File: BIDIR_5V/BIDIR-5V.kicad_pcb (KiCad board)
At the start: 2 copper layers, 5 x 34 mm, 16 parts, among them U1 SN74LVC1T45DCK

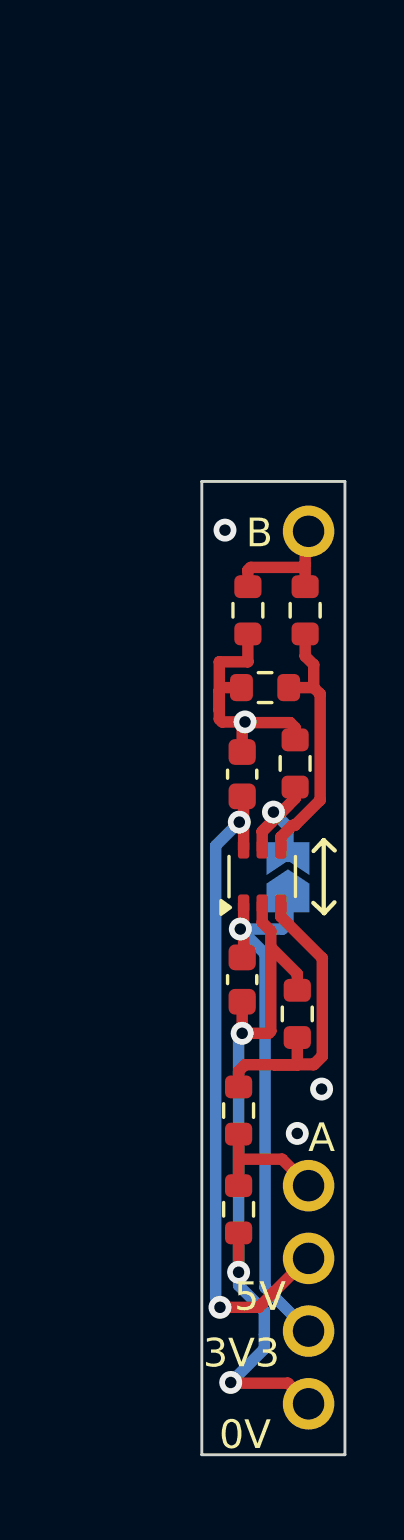
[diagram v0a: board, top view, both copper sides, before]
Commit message: retouche pour 10mm de large
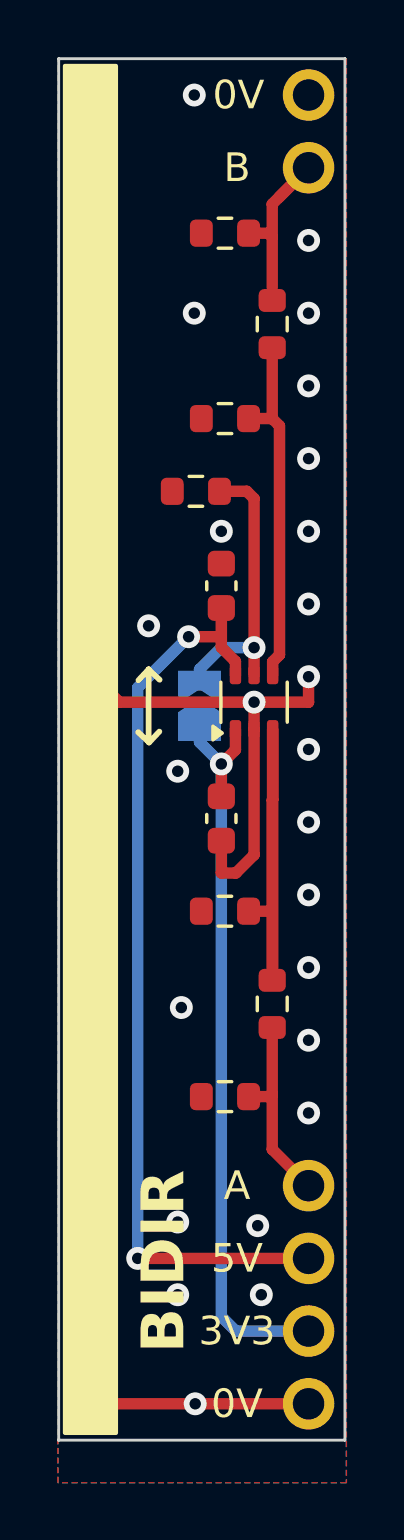
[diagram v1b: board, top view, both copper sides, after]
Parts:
- added TP6: TestPoint, Chimere_comps:Pastille, F.Cu at (248.9, 50.8)
- moved R7 13.2 mm to (246.0, 55.6), turned to 180 degrees
- moved TP1 12.7 mm to (248.9, 53.3)
- moved R4 10.1 mm to (245.0, 64.6), turned to 180 degrees
- moved R6 10.1 mm to (247.7, 58.8)
- moved R5 9.50 mm to (246.0, 62.1)
- moved JP1 6.74 mm to (245.1, 72.1)
- moved C2 6.62 mm to (245.9, 67.9)
- moved U1 6.10 mm to (247.0, 72.0)
- moved C1 5.67 mm to (245.9, 76.1)
- moved R3 4.39 mm to (246.0, 79.3), turned to 180 degrees
- moved R1 3.96 mm to (246.0, 85.8), turned to 180 degrees
- moved R2 3.91 mm to (247.7, 82.5)
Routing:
- net /GND: track 35.9 -> 24.1 mm, vias 7 -> 44
- net /5V: track 22.7 -> 32.1 mm
- net /3V3: track 19.6 -> 26.7 mm
- net Net-(U1-A): track 12.4 -> 18.4 mm
- net Net-(JP1-B): track 6.28 -> 10.2 mm
- net Net-(U1-B): track 9.23 -> 12.5 mm
- net /OUT: track 4.47 -> 7.03 mm
- net /OUT_i: track 4.63 -> 6.90 mm
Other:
- board size 5 x 34 mm -> 10 x 48.3 mm
- board text added: "2025/10/30"
- board text added: "BIDIR"
- board text removed: "2024/11/22"
